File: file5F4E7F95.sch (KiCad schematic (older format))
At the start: 8 parts

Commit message: cascading regulators done
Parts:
- added C? (x2): 10uF 12V, symbol Device:C
- added C? (x2): 100nF, symbol Device:C
- added C? (x2): 22uF 3.3v, symbol Device:C
- added C? (x2): 22uF 5v, symbol Device:C
- added L? (x2): 3.3uH, symbol Device:L
- added R?: 31.6k, symbol Device:R
- added R? (x2): 10k, symbol Device:R
- added R?: 52.3k, symbol Device:R
- added U? (x2): AP62300, Package_TO_SOT_SMD:SOT-563, symbol my_parts:AP62300
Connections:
- net +12V: now also C?.1, C?.1, U?.3 (Vin), U?.3 (Vin)
- net GND: now also C?.2, C?.2, C?.2, C?.2, C?.2, C?.2, R?.2, R?.2, U?.1 (GND), U?.1 (GND)
- new net: C?.1, U?.6 (BST) (x2)
- new net: C?.2, L?.1, U?.2 (SW) (x2)
- new net: R?.1, R?.2, U?.4 (FB) (x2)
- new net +3V3: C?.1, C?.1, L?.2, R?.1
- new net +5V: C?.1, C?.1, L?.2, R?.1
- no-connect marks 2 -> 4
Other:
- note added: "3.3v reg 3A 9.9w"
- note added: "5v reg 3A 15w"
- note added: "A higher current regulator with an external fet is availabel from the same manufacturer"

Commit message: Time for layout!
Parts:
- C10, C9: renamed from C?; value 100nF -> 100nF X5R 6V; footprint (none) -> Capacitor_SMD:C_0805_2012Metric
- C12, C14: renamed from C?; value 22uF 5v -> 22uF X7R 10v; footprint (none) -> Capacitor_SMD:C_0805_2012Metric
- C13, C15: renamed from C?; value 22uF 3.3v -> 22uF X7R 10v; footprint (none) -> Capacitor_SMD:C_0805_2012Metric
- C3, C5, C6, C7, C8: renamed from C?; footprint (none) -> Capacitor_SMD:C_0805_2012Metric
- C4: renamed from C?; value 1uF -> 1uF X5R 5v; footprint (none) -> Capacitor_SMD:C_0805_2012Metric
- L1: renamed from L?; footprint (none) -> Inductor_SMD:L_Wuerth_WE-PD-Typ-LS
- L2, L3: renamed from L?; footprint (none) -> Inductor_SMD:L_Vishay_IHLP-2020
- R10, R11, R12, R13, R8, R9: renamed from R?; footprint (none) -> Resistor_SMD:R_0805_2012Metric
- U3: renamed from U?; footprint (none) -> Package_DFN_QFN:QFN-36-1EP_5x6mm_P0.5mm_EP3.6x4.6mm_ThermalVias
- gave numbers to parts that had none: 2

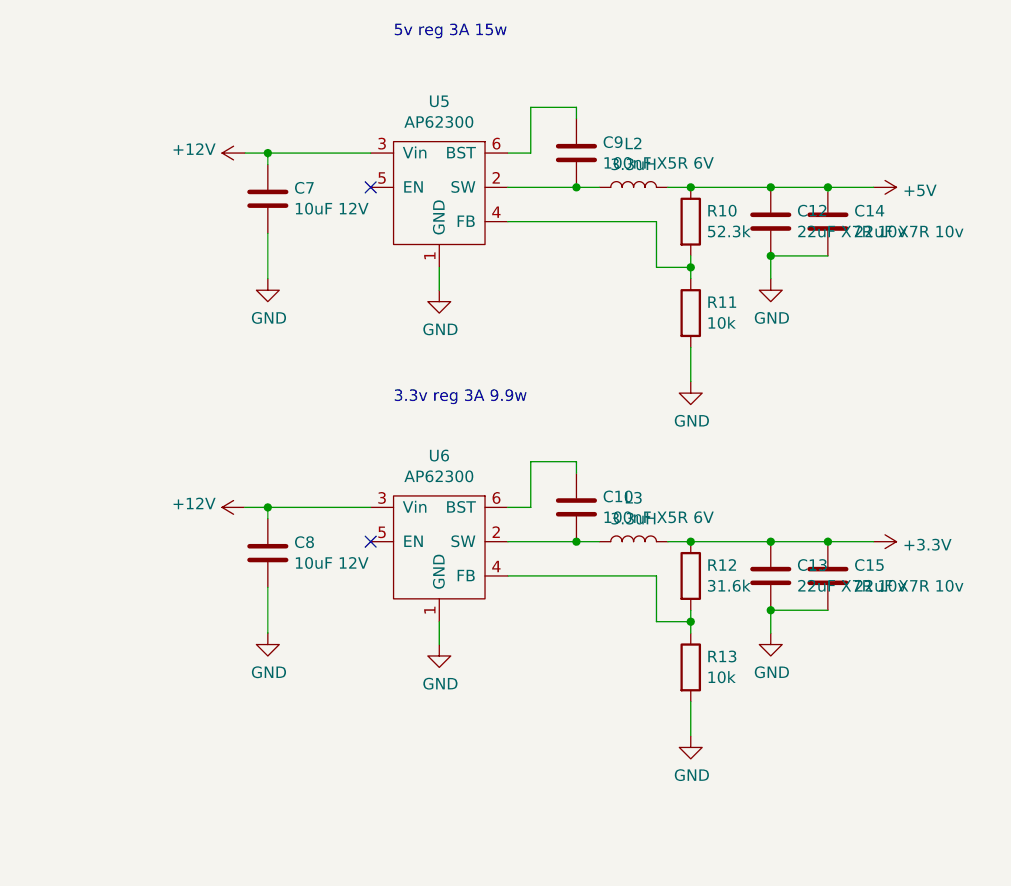
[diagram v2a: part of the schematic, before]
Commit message: 5v +3.3v reg layed out
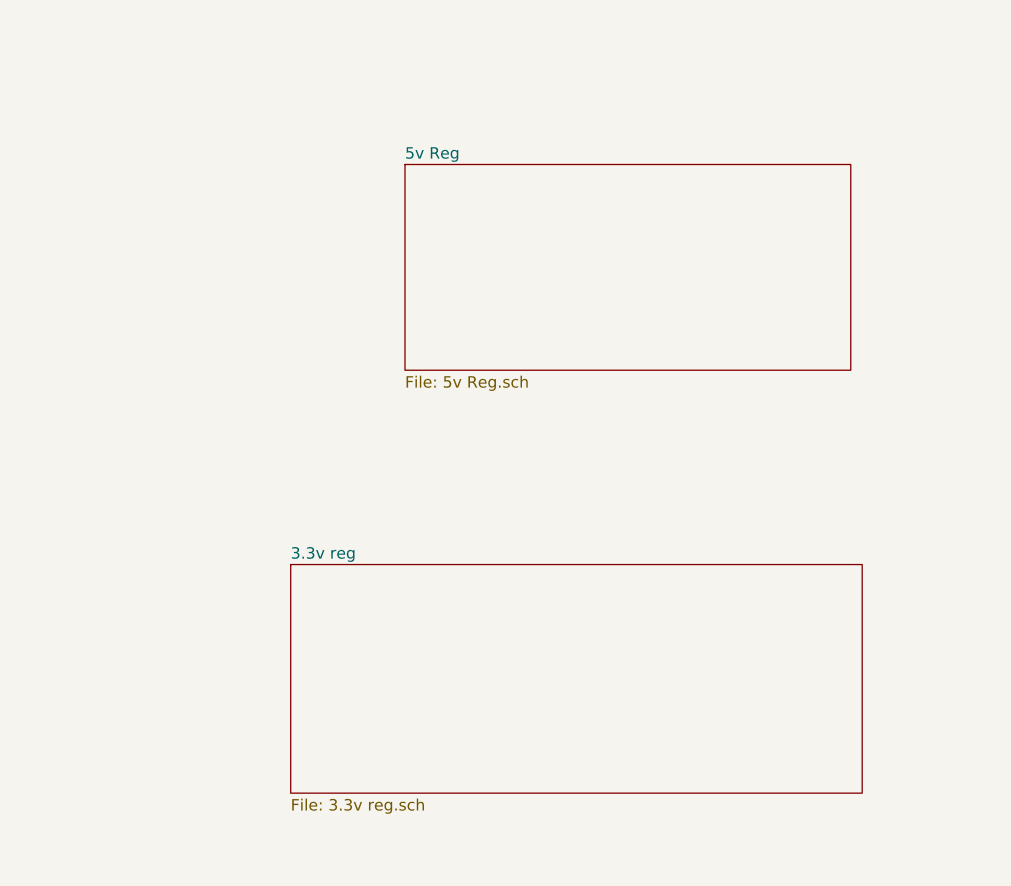
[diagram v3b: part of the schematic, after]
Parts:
- removed C10, C9: 100nF X5R 6V, Capacitor_SMD:C_0805_2012Metric, symbol Device:C
- removed C12, C13, C14, C15: 22uF X7R 10v, Capacitor_SMD:C_0805_2012Metric, symbol Device:C
- removed C7, C8: 10uF 12V, Capacitor_SMD:C_0805_2012Metric, symbol Device:C
- removed L2, L3: 3.3uH, Inductor_SMD:L_Vishay_IHLP-2020, symbol Device:L
- removed R10: 52.3k, Resistor_SMD:R_0805_2012Metric, symbol Device:R
- removed R11, R13: 10k, Resistor_SMD:R_0805_2012Metric, symbol Device:R
- removed R12: 31.6k, Resistor_SMD:R_0805_2012Metric, symbol Device:R
- removed U5, U6: AP62300, Package_TO_SOT_SMD:SOT-563, symbol my_parts:AP62300
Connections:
- no-connect marks 4 -> 2
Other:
- note removed: "3.3v reg 3A 9.9w"
- note removed: "5v reg 3A 15w"

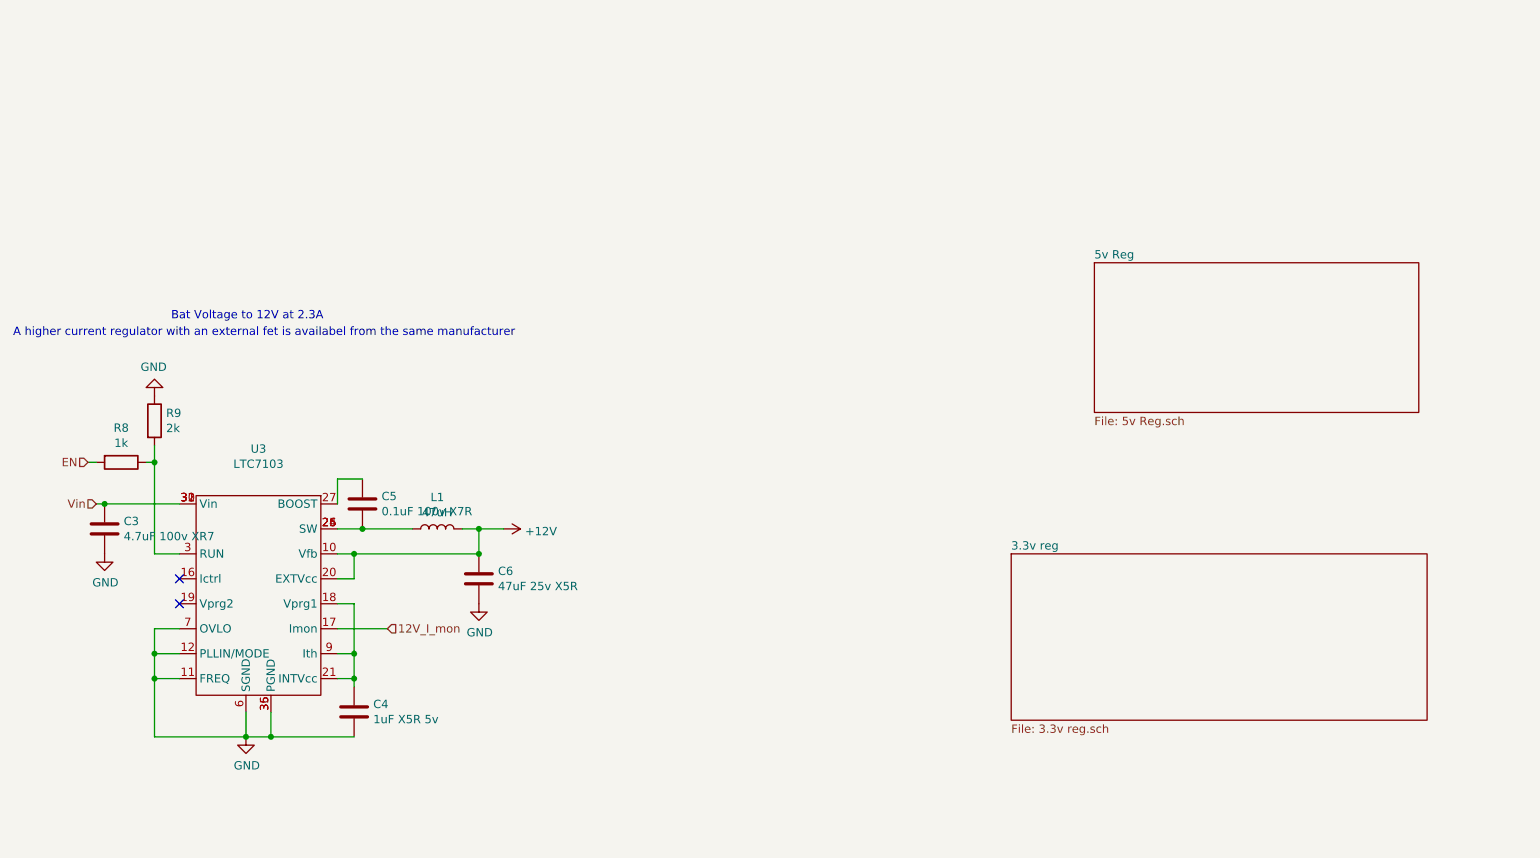
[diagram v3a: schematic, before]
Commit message: 2 12v reg v
(cherry picked from commit e80781844bee15763a75ec210b83760850c4e868)
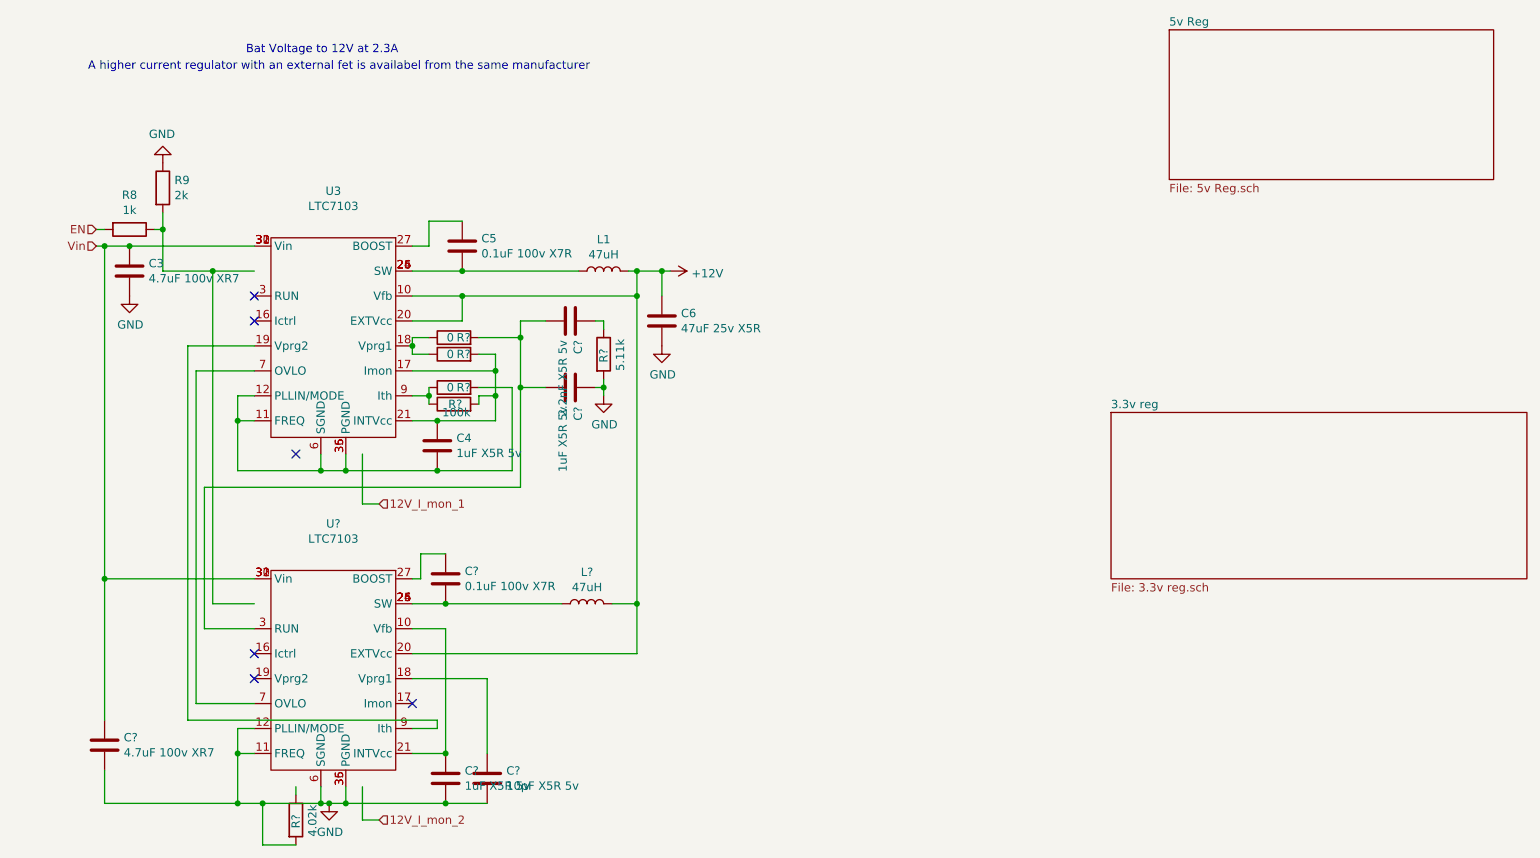
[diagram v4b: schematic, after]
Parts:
- added C?: 4.7uF 100v XR7, Capacitor_SMD:C_0805_2012Metric, symbol Device:C
- added C?: 2.2nF X5R 5v, Capacitor_SMD:C_0805_2012Metric, symbol Device:C
- added C? (x2): 1uF X5R 5v, Capacitor_SMD:C_0805_2012Metric, symbol Device:C
- added C?: 10pF X5R 5v, Capacitor_SMD:C_0805_2012Metric, symbol Device:C
- added C?: 0.1uF 100v X7R, Capacitor_SMD:C_0805_2012Metric, symbol Device:C
- added L?: 47uH, Inductor_SMD:L_Wuerth_WE-PD-Typ-LS, symbol Device:L
- added R?: 100k, Resistor_SMD:R_0805_2012Metric, symbol Device:R
- added R? (x3): 0, Resistor_SMD:R_0805_2012Metric, symbol Device:R
- added R?: 5.11k, Resistor_SMD:R_0805_2012Metric, symbol Device:R
- added R?: 4.02k, Resistor_SMD:R_0805_2012Metric, symbol Device:R
- added U?: LTC7103, Package_DFN_QFN:QFN-36-1EP_5x6mm_P0.5mm_EP3.6x4.6mm_ThermalVias, symbol my_parts:LTC7103
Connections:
- net labels added: 12V_I_mon_1, 12V_I_mon_2
- net labels removed: 12V_I_mon
- wire segments 36 -> 113
- no-connect marks 2 -> 6
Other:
- moved on the sheet: C3, C4, C5, C6, L1, R8, R9, U3

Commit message: Revert "2 12v reg v"
This reverts commit 039d006401861a5917fcf1b07647dbdfad4f578a.
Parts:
- removed C?: 4.7uF 100v XR7, Capacitor_SMD:C_0805_2012Metric, symbol Device:C
- removed C?: 2.2nF X5R 5v, Capacitor_SMD:C_0805_2012Metric, symbol Device:C
- removed C? (x2): 1uF X5R 5v, Capacitor_SMD:C_0805_2012Metric, symbol Device:C
- removed C?: 10pF X5R 5v, Capacitor_SMD:C_0805_2012Metric, symbol Device:C
- removed C?: 0.1uF 100v X7R, Capacitor_SMD:C_0805_2012Metric, symbol Device:C
- removed L?: 47uH, Inductor_SMD:L_Wuerth_WE-PD-Typ-LS, symbol Device:L
- removed R?: 100k, Resistor_SMD:R_0805_2012Metric, symbol Device:R
- removed R? (x3): 0, Resistor_SMD:R_0805_2012Metric, symbol Device:R
- removed R?: 5.11k, Resistor_SMD:R_0805_2012Metric, symbol Device:R
- removed R?: 4.02k, Resistor_SMD:R_0805_2012Metric, symbol Device:R
- removed U?: LTC7103, Package_DFN_QFN:QFN-36-1EP_5x6mm_P0.5mm_EP3.6x4.6mm_ThermalVias, symbol my_parts:LTC7103
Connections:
- net labels added: 12V_I_mon
- net labels removed: 12V_I_mon_1, 12V_I_mon_2
- wire segments 113 -> 36
- no-connect marks 6 -> 2
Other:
- moved on the sheet: C3, C4, C5, C6, L1, R8, R9, U3
